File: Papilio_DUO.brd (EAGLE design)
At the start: 100 x 56 mm, 112 parts, among them IC1 FT2232H, SW1 SWITCH-2CH-6P-3010010P1, SW2 EVQQ2, U1 ARDUINO_MEGA_SHIELD, U101 ATMEGA32U4-XUMU, U2 LTC3419EMS, U3 93C46B, X1 12MHz, Y1 16MHz KX-7

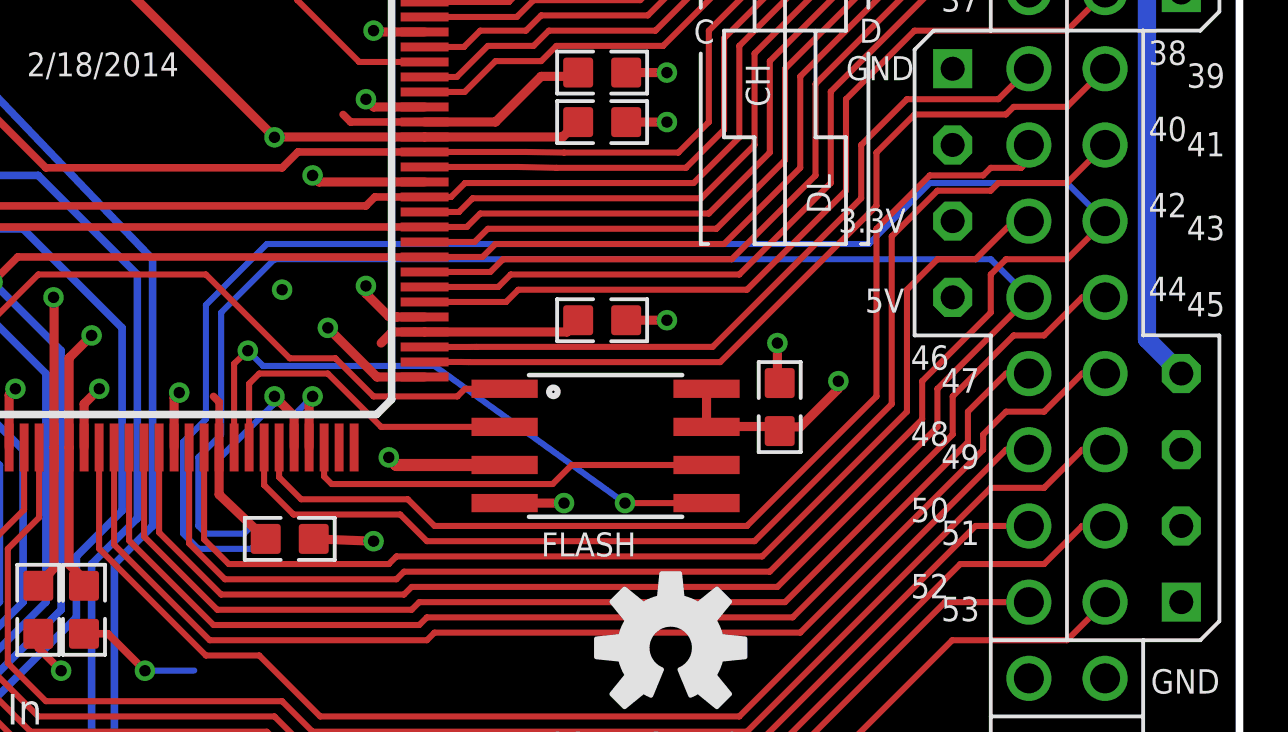
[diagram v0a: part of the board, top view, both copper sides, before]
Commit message: Cleaned up some HDMI traces.
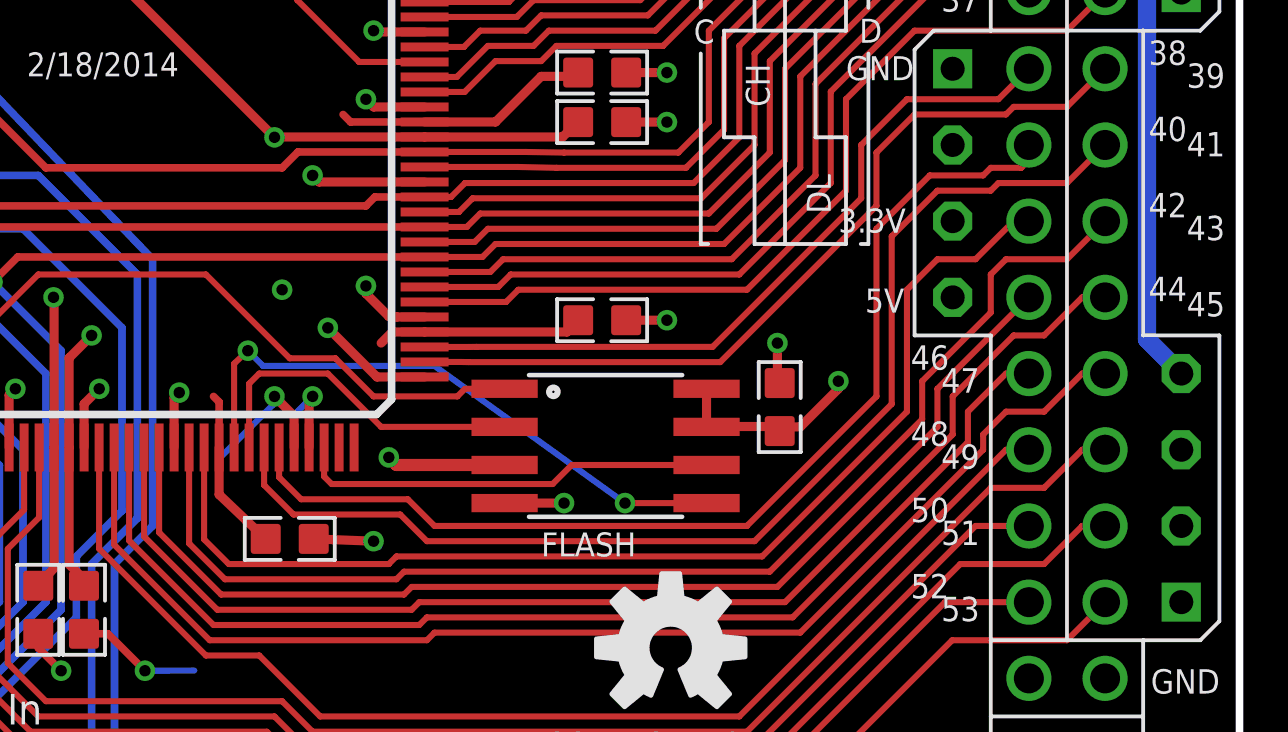
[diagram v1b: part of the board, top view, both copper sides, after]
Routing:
- net MEGA_D43: track 83.9 -> 40.7 mm
- net MEGA_D44: track 75.0 -> 37.5 mm
- net 5V0: track 299.7 -> 277.1 mm
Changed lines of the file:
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@@
 <layer number="19" name="Unrouted" color="12" fill="1" visible="yes" active="yes"/>
 <layer number="20" name="Dimension" color="15" fill="1" visible="yes" active="yes"/>
-<layer number="21" name="tPlace" color="25" fill="1" visible="no" active="yes"/>
-<layer number="22" name="bPlace" color="13" fill="1" visible="no" active="yes"/>
-<layer number="23" name="tOrigins" color="15" fill="1" visible="no" active="yes"/>
-<layer number="24" name="bOrigins" color="15" fill="1" visible="no" active="yes"/>
-<layer number="25" name="tNames" color="7" fill="1" visible="no" active="yes"/>
+<layer number="21" name="tPlace" color="25" fill="1" visible="yes" active="yes"/>
+<layer number="22" name="bPlace" color="13" fill="1" visible="yes" active="yes"/>
+<layer number="23" name="tOrigins" color="15" fill="1" visible="yes" active="yes"/>
+<layer number="24" name="bOrigins" color="15" fill="1" visible="yes" active="yes"/>
+<layer number="25" name="tNames" color="7" fill="1" visible="yes" active="yes"/>
 <layer number="26" name="bNames" color="7" fill="1" visible="no" active="yes"/>
 <layer number="27" name="tValues" color="7" fill="1" visible="no" active="yes"/>
@@
 <layer number="127" name="_tValues" color="7" fill="1" visible="no" active="no"/>
 <layer number="128" name="_bValues" color="7" fill="1" visible="no" active="no"/>
-<layer number="130" name="tSilk" color="7" fill="1" visible="yes" active="yes"/>
+<layer number="130" name="tSilk" color="7" fill="1" visible="no" active="yes"/>
 <layer number="131" name="prix" color="7" fill="1" visible="no" active="yes"/>
 <layer number="132" name="test" color="7" fill="1" visible="no" active="yes"/>
@@
 <wire x1="64.988" y1="15.316" x2="64.988" y2="12.117" width="0.2032" layer="1"/>
 <wire x1="64.988" y1="12.117" x2="66.183" y2="10.922" width="0.2032" layer="1"/>
-<wire x1="67.502" y1="12.368" x2="67.072" y2="11.938" width="0.2032" layer="16"/>
-<wire x1="67.072" y1="11.938" x2="65.294" y2="11.938" width="0.2032" layer="16"/>
-<wire x1="65.294" y1="11.938" x2="64.786" y2="12.446" width="0.2032" layer="16"/>
-<wire x1="64.786" y1="12.446" x2="64.786" y2="15.494" width="0.2032" layer="16"/>
-<wire x1="64.786" y1="15.494" x2="65.548" y2="16.256" width="0.2032" layer="16"/>
-<wire x1="65.548" y1="16.256" x2="65.548" y2="20.066" width="0.2032" layer="16"/>
-<wire x1="65.548" y1="20.066" x2="67.58" y2="22.098" width="0.2032" layer="16"/>
-<wire x1="67.58" y1="22.098" x2="87.646" y2="22.098" width="0.2032" layer="16"/>
-<wire x1="87.646" y1="22.098" x2="89.678" y2="24.13" width="0.2032" layer="16"/>
-<wire x1="89.678" y1="24.13" x2="94.25" y2="24.13" width="0.2032" layer="16"/>
-<wire x1="94.25" y1="24.13" x2="95.52" y2="22.86" width="0.2032" layer="16"/>
 <wire x1="66.183" y1="10.922" x2="71.898" y2="10.922" width="0.2032" layer="1"/>
 <wire x1="71.898" y1="10.922" x2="72.152" y2="11.176" width="0.2032" layer="1"/>
@@
 <wire x1="63.988" y1="15.316" x2="63.988" y2="12.482" width="0.2032" layer="1"/>
 <wire x1="63.988" y1="12.482" x2="66.056" y2="10.414" width="0.2032" layer="1"/>
-<wire x1="67.002" y1="12.63" x2="66.818" y2="12.446" width="0.2032" layer="16"/>
-<wire x1="66.818" y1="12.446" x2="65.548" y2="12.446" width="0.2032" layer="16"/>
-<wire x1="65.548" y1="12.446" x2="65.294" y2="12.7" width="0.2032" layer="16"/>
-<wire x1="67.834" y1="21.59" x2="91.71" y2="21.59" width="0.2032" layer="16"/>
-<wire x1="91.71" y1="21.59" x2="92.98" y2="20.32" width="0.2032" layer="16"/>
-<wire x1="65.294" y1="12.7" x2="65.294" y2="14.986" width="0.2032" layer="16"/>
-<wire x1="65.294" y1="14.986" x2="66.056" y2="15.748" width="0.2032" layer="16"/>
-<wire x1="66.056" y1="15.748" x2="66.056" y2="19.812" width="0.2032" layer="16"/>
-<wire x1="66.056" y1="19.812" x2="67.834" y2="21.59" width="0.2032" layer="16"/>
 <wire x1="66.056" y1="10.414" x2="72.152" y2="10.414" width="0.2032" layer="1"/>
 <wire x1="72.152" y1="10.414" x2="72.406" y2="10.668" width="0.2032" layer="1"/>
@@
 <wire x1="96.79" y1="21.59" x2="91.71" y2="21.59" width="0.4064" layer="3"/>
 <wire x1="91.71" y1="21.59" x2="90.44" y2="20.32" width="0.4064" layer="3"/>
-<wire x1="73.7268" y1="8.3566" x2="73.7268" y2="8.6868" width="0.4064" layer="3"/>
-<wire x1="73.7268" y1="8.6868" x2="75.2" y2="10.16" width="0.4064" layer="3"/>
-<wire x1="75.2" y1="10.16" x2="81.55" y2="10.16" width="0.4064" layer="3"/>
-<wire x1="81.55" y1="10.16" x2="90.44" y2="19.05" width="0.4064" layer="3"/>
-<wire x1="90.44" y1="19.05" x2="90.44" y2="20.32" width="0.4064" layer="3"/>
 <wire x1="37.1" y1="2.54" x2="37.1" y2="2.032" width="1.016" layer="3"/>
 <wire x1="37.1" y1="2.032" x2="36.084" y2="1.016" width="1.016" layer="3"/>

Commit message: Added Headers to the BOM
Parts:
- WING_POWER1, WING_POWER2, WING_POWER3, WING_POWER4, WING_POWER5, WING_POWER6: value POWER_ONLYNOTEXT -> HEADER_FEMALE_4
- renumbered U$2 to WING_POWER1, U$3 to WING_POWER4, U$4 to WING_POWER5, U$5 to WING_POWER3, U$6 to WING_POWER6, U$8 to WING_POWER2
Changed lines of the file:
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@@
 <attribute name="PARTNO" value="PTS525SM10SMTR LFS" x="31.512" y="11.938" size="1.778" layer="27" display="off"/>
 </element>
-<element name="U$2" library="Papilio" package="POWER_NO_TEXT" value="POWER_ONLYNOTEXT" x="58.69" y="53.34" smashed="yes" rot="R270">
-<attribute name="BOM" value="EXCLUDE" x="58.69" y="53.34" size="1.778" layer="27" rot="R270" display="off"/>
-</element>
-<element name="U$8" library="Papilio" package="POWER_NO_TEXT" value="POWER_ONLYNOTEXT" x="98.06" y="13.97" smashed="yes" rot="R180">
-<attribute name="BOM" value="EXCLUDE" x="98.06" y="13.97" size="1.778" layer="27" rot="R180" display="off"/>
-</element>
-<element name="U$5" library="Papilio" package="POWER_NO_TEXT" value="POWER_ONLYNOTEXT" x="98.06" y="34.29" smashed="yes" rot="R180">
-<attribute name="BOM" value="EXCLUDE" x="98.06" y="34.29" size="1.778" layer="27" rot="R180" display="off"/>
-</element>
-<element name="U$3" library="Papilio" package="POWER_NO_TEXT" value="POWER_ONLYNOTEXT" x="81.55" y="53.34" smashed="yes" rot="R270">
-<attribute name="BOM" value="EXCLUDE" x="81.55" y="53.34" size="1.778" layer="27" rot="R270" display="off"/>
-</element>
-<element name="U$4" library="Papilio" package="POWER_NO_TEXT" value="POWER_ONLYNOTEXT" x="90.44" y="44.45" smashed="yes">
-<attribute name="BOM" value="EXCLUDE" x="90.44" y="44.45" size="1.778" layer="27" display="off"/>
-</element>
-<element name="U$6" library="Papilio" package="POWER_NO_TEXT" value="POWER_ONLYNOTEXT" x="90.44" y="24.13" smashed="yes">
-<attribute name="BOM" value="EXCLUDE" x="90.44" y="24.13" size="1.778" layer="27" display="off"/>
+<element name="WING_POWER1" library="Papilio" package="POWER_NO_TEXT" value="HEADER_FEMALE_4" x="58.69" y="53.34" smashed="yes" rot="R270">
+<attribute name="PARTNO" value="PPTC041LFBN-RC" x="58.69" y="53.34" size="1.778" layer="27" rot="R270" display="off"/>
+</element>
+<element name="WING_POWER2" library="Papilio" package="POWER_NO_TEXT" value="HEADER_FEMALE_4" x="98.06" y="13.97" smashed="yes" rot="R180">
+<attribute name="PARTNO" value="PPTC041LFBN-RC" x="98.06" y="13.97" size="1.778" layer="27" rot="R180" display="off"/>
+</element>
+<element name="WING_POWER3" library="Papilio" package="POWER_NO_TEXT" value="HEADER_FEMALE_4" x="98.06" y="34.29" smashed="yes" rot="R180">
+<attribute name="PARTNO" value="PPTC041LFBN-RC" x="98.06" y="34.29" size="1.778" layer="27" rot="R180" display="off"/>
+</element>
+<element name="WING_POWER4" library="Papilio" package="POWER_NO_TEXT" value="HEADER_FEMALE_4" x="81.55" y="53.34" smashed="yes" rot="R270">
+<attribute name="PARTNO" value="PPTC041LFBN-RC" x="81.55" y="53.34" size="1.778" layer="27" rot="R270" display="off"/>
+</element>
+<element name="WING_POWER5" library="Papilio" package="POWER_NO_TEXT" value="HEADER_FEMALE_4" x="90.44" y="44.45" smashed="yes">
+<attribute name="PARTNO" value="PPTC041LFBN-RC" x="90.44" y="44.45" size="1.778" layer="27" display="off"/>
+</element>
+<element name="WING_POWER6" library="Papilio" package="POWER_NO_TEXT" value="HEADER_FEMALE_4" x="90.44" y="24.13" smashed="yes">
+<attribute name="PARTNO" value="PPTC041LFBN-RC" x="90.44" y="24.13" size="1.778" layer="27" display="off"/>
 </element>
 <element name="U1" library="GadgetFactory_tmp" package="ARDUINO_MEGA_SHIELD" value="ARDUINO_MEGA_SHIELD" x="7.89" y="53.34" smashed="yes" rot="R270">
@@
 <contactref element="SW2" pad="B'"/>
 <contactref element="SW2" pad="B"/>
-<contactref element="U$2" pad="P1"/>
-<contactref element="U$8" pad="P1"/>
-<contactref element="U$5" pad="P1"/>
-<contactref element="U$3" pad="P1"/>
-<contactref element="U$4" pad="P1"/>
-<contactref element="U$6" pad="P1"/>
+<contactref element="WING_POWER1" pad="P1"/>
+<contactref element="WING_POWER2" pad="P1"/>
+<contactref element="WING_POWER3" pad="P1"/>
+<contactref element="WING_POWER4" pad="P1"/>
+<contactref element="WING_POWER5" pad="P1"/>
+<contactref element="WING_POWER6" pad="P1"/>
 <contactref element="U$1" pad="JTAG_GND"/>
 <wire x1="68.488" y1="36.087" x2="68.488" y2="37.516" width="0.3048" layer="1"/>
@@
 <contactref element="C24" pad="1"/>
 <contactref element="R31" pad="2"/>
-<contactref element="U$2" pad="P3"/>
-<contactref element="U$8" pad="P3"/>
-<contactref element="U$5" pad="P3"/>
-<contactref element="U$3" pad="P3"/>
-<contactref element="U$4" pad="P3"/>
-<contactref element="U$6" pad="P3"/>
+<contactref element="WING_POWER1" pad="P3"/>
+<contactref element="WING_POWER2" pad="P3"/>
+<contactref element="WING_POWER3" pad="P3"/>
+<contactref element="WING_POWER4" pad="P3"/>
+<contactref element="WING_POWER5" pad="P3"/>
+<contactref element="WING_POWER6" pad="P3"/>
 <contactref element="U1" pad="3.3V"/>
 <contactref element="U$1" pad="JTAG_REF"/>
@@
 </signal>
 <signal name="5V0">
-<contactref element="U$2" pad="P4"/>
-<contactref element="U$8" pad="P4"/>
-<contactref element="U$5" pad="P4"/>
-<contactref element="U$3" pad="P4"/>
-<contactref element="U$4" pad="P4"/>
-<contactref element="U$6" pad="P4"/>
+<contactref element="WING_POWER1" pad="P4"/>
+<contactref element="WING_POWER2" pad="P4"/>
+<contactref element="WING_POWER3" pad="P4"/>
+<contactref element="WING_POWER4" pad="P4"/>
+<contactref element="WING_POWER5" pad="P4"/>
+<contactref element="WING_POWER6" pad="P4"/>
 <contactref element="U1" pad="5V@0"/>
 <wire x1="98.06" y1="38.1" x2="96.79" y2="39.37" width="0.4064" layer="16"/>

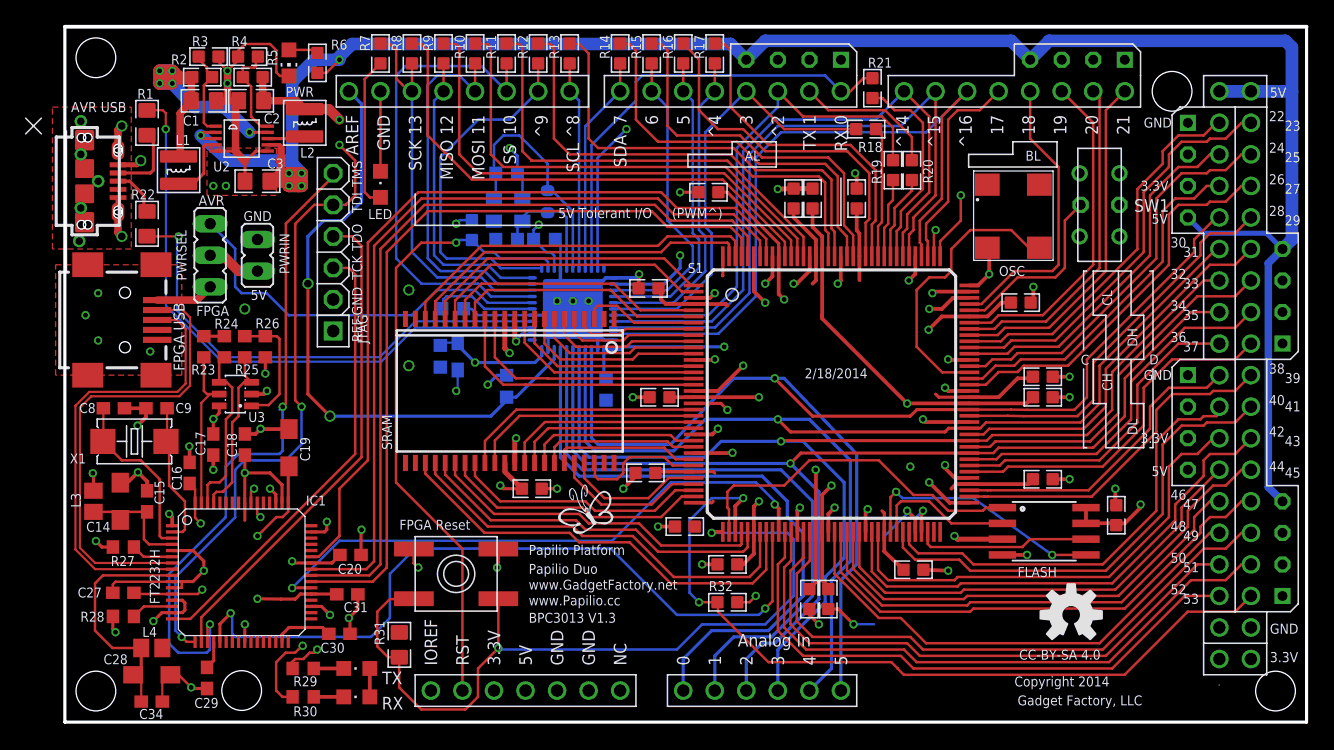
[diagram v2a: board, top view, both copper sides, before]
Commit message: Papilio DUO V1.4
Fixed the mounting holes.
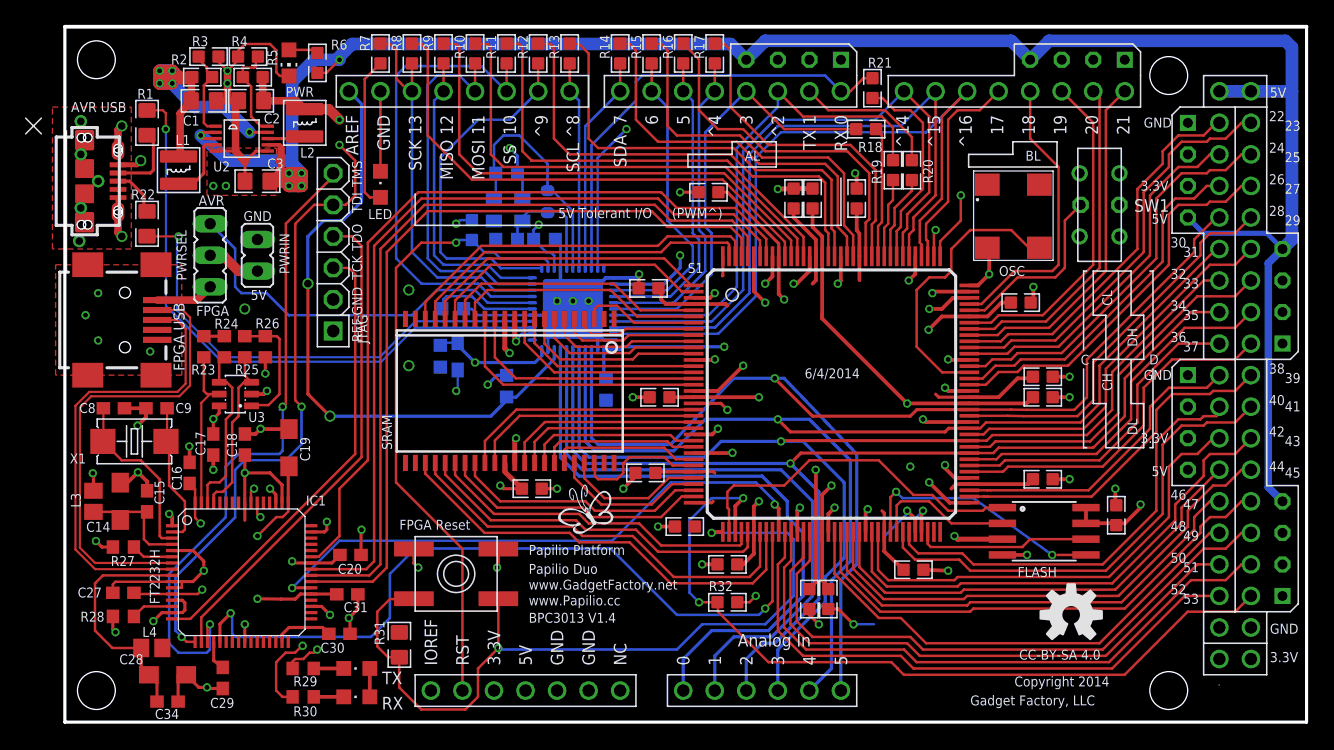
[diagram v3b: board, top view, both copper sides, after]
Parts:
- added U$2, U$3, U$4, U$5: (no value), SparkFun:STAND-OFF-TIGHT
- SRAM: value ISSI_SRAM_8BIT -> (none)
- moved C28 1.27 mm to (8.27, 3.81)
- moved C34 1.27 mm to (8.27, 1.65)
- moved C29 1.27 mm to (12.7, 3.56)
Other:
- board text added: "6/4/2014"
- board text added: "BPC3013 V1.4"
- board text removed: "2/18/2014"
- board text removed: "BPC3013 V1.3"
